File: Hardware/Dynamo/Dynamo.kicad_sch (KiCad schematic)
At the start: 50 parts, among them U1 AP63205WU, U10 ESP32-S3-WROOM-1, U11 NCP1117-3.3_SOT223, U12 74AHC1G32, U13 TXS0102DCT, U14 TXS0102DCT, U15 74AHC1G32, U16 74AHC1G32, U17 74AHC1G32, U2 TLP2770, U3 TLP2770, U4 74LVC1G86, U5 74LVC1G86, U6 74LVC1G86, U7 74LVC1G86, U8 74LVC1G86, U9 74LVC1G86

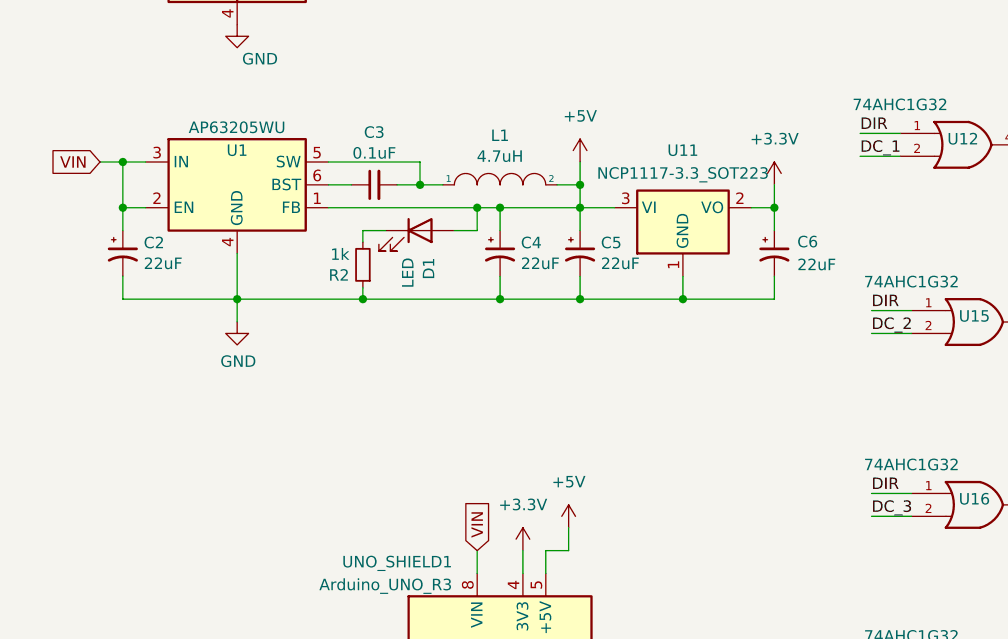
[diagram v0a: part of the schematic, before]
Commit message: Revised 5v regulator, layout refinement.
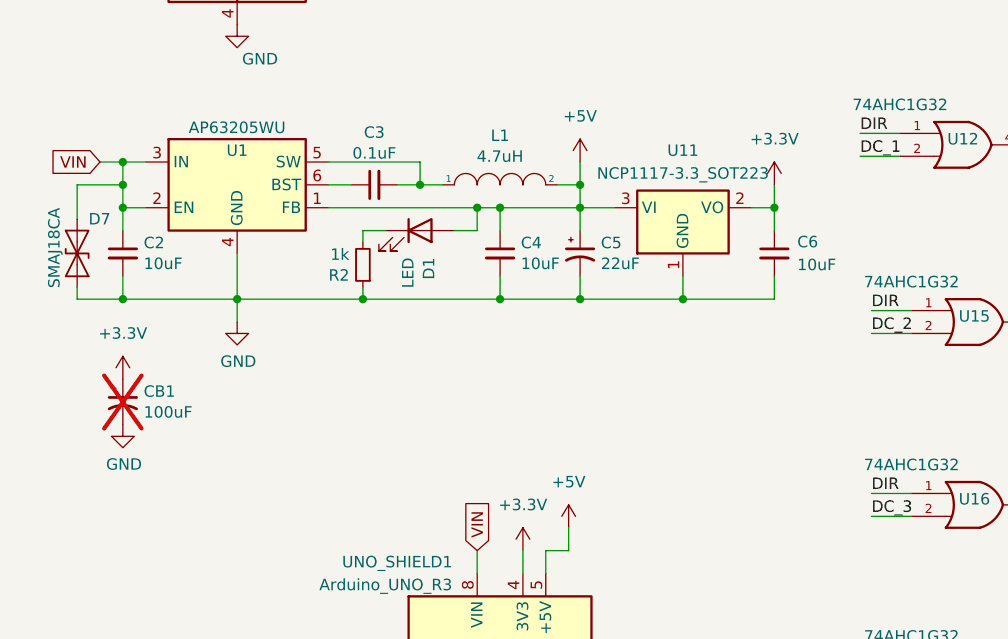
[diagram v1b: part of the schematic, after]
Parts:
- added CB1: 100uF, Capacitor_THT:CP_Radial_D6.3mm_P2.50mm, symbol Motor Shield Adapter-rescue:CP1_Small-Device
- added D7: SMAJ18CA, Diode_SMD:D_SMA, symbol Diode:SMAJ18CA
- C2, C4: value 22uF -> 10uF; footprint Capacitor_SMD:CP_Elec_5x5.3 -> Capacitor_SMD:C_1210_3225Metric; symbol Motor Shield Adapter-rescue:CP1_Small-Device -> Device:C_Small; JLCPCB Part # C2164091 -> C2175202; MFG Wurth Electronik -> Murata; PN 865080542006 -> GRT31CR6YA106ME01L
- C6: value 22uF -> 10uF; footprint Capacitor_SMD:CP_Elec_5x5.3 -> Capacitor_SMD:C_1210_3225Metric; symbol Device:C_Polarized_Small_US -> Device:C_Small; JLCPCB Part # C2164091 -> C2175202; MFG Wurth Electronik -> Murata; PN 865080542006 -> GRT31CR6YA106ME01L
- L1: JLCPCB Part # (none) -> C2045329
- U12, U15, U16, U17: MFG (none) -> Texas Insturments
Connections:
- net +3.3V: now also CB1.1
- net GND: now also CB1.2, D7.2 (A2)
- net VIN: now also D7.1 (A1)

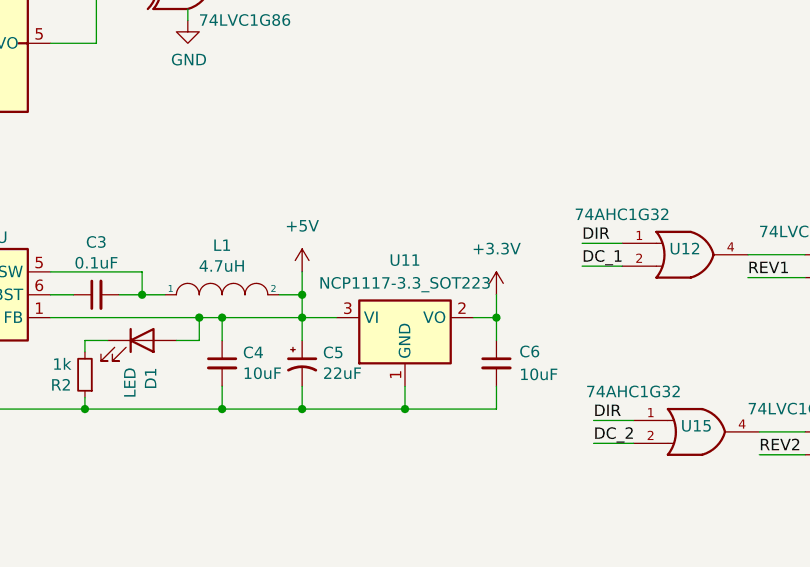
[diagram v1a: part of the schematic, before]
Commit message: BOM fix, replace NCP1117 with TLV1117
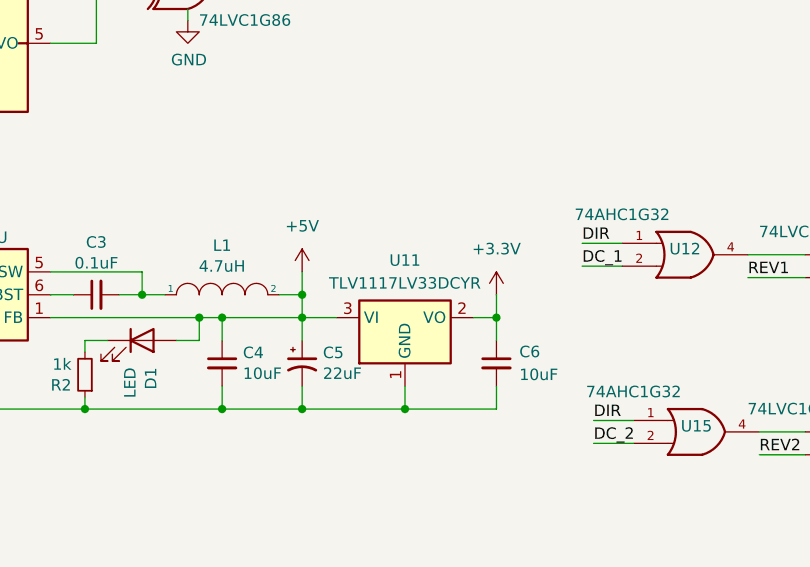
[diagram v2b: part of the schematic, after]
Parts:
- U11: value NCP1117-3.3_SOT223 -> TLV1117LV33DCYR; MFG ONSemi -> Texas Insturments; PN NCP1117ST33T3G -> TLV1117LV33DCYR
- UNO_SHIELD1: MFG (none) -> Arduino; PN (none) -> 85
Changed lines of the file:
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@@
+      (effects (font (size 1.27 1.27)) hide)
+    )
+    (property "MFG" "Arduino" (at 67.31 157.48 0)
+      (effects (font (size 1.27 1.27)) hide)
+    )
+    (property "PN" "85" (at 67.31 157.48 0)
       (effects (font (size 1.27 1.27)) hide)
     )
@@
       (effects (font (size 1.27 1.27)))
     )
-    (property "Value" "NCP1117-3.3_SOT223" (at 87.63 87.63 0)
+    (property "Value" "TLV1117LV33DCYR " (at 87.63 87.63 0)
       (effects (font (size 1.27 1.27)))
     )
@@
       (effects (font (size 1.27 1.27)) hide)
     )
-    (property "Datasheet" "http://www.onsemi.com/pub_link/Collateral/NCP1117-D.PDF" (at 90.17 97.79 0)
-      (effects (font (size 1.27 1.27)) hide)
-    )
-    (property "MFG" "ONSemi" (at 87.63 91.44 0)
-      (effects (font (size 1.27 1.27)) hide)
-    )
-    (property "PN" "NCP1117ST33T3G" (at 87.63 91.44 0)
-      (effects (font (size 1.27 1.27)) hide)
-    )
+    (property "Datasheet" "https://www.ti.com/lit/gpn/tlv1117lv" (at 90.17 97.79 0)
+      (effects (font (size 1.27 1.27)) hide)
+    )
+    (property "MFG" "Texas Insturments" (at 87.63 91.44 0)
+      (effects (font (size 1.27 1.27)) hide)
+    )
+    (property "PN" "TLV1117LV33DCYR " (at 87.63 91.44 0)
+      (effects (font (size 1.27 1.27)) hide)
+    )
